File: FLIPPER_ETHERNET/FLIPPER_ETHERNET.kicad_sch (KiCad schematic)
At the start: 21 parts, among them J1 RJ45_Hanrun_HR911105A_Horizon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, J2 Conn_01x08_Socket, J3 Conn_01x10_Socket, SW1 SW_Push, U1 ENC28J60x-ML, Y1 25MHz

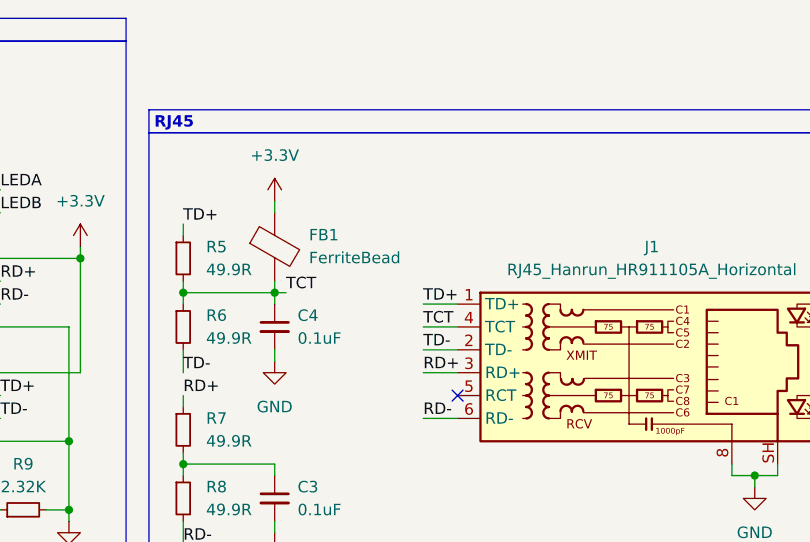
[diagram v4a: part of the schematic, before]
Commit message: feat: bom corrected and change of model components components changed were SW1 and FB1
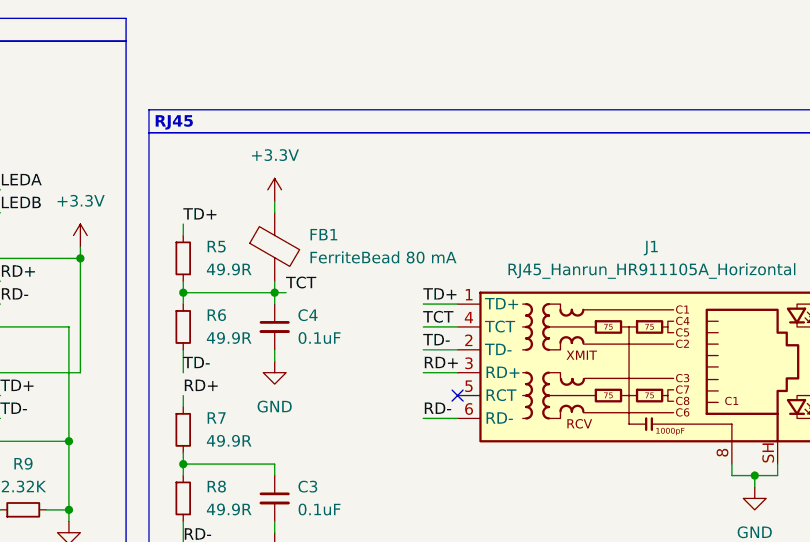
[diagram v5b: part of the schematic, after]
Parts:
- C1, C5: #LSCS C3870208 -> C107040; manf# 600S180FT250XT -> CC0603JRNPO9BN180
- C2: #LSCS C192094 -> C1691; manf# GRM188R60J106ME84D -> CL10A106MQ8NNNC
- C3, C4: #LSCS C20214933 -> C14663; manf# KGF15AR71E104JT -> CC0603KRX7R9BB104
- FB1: value FerriteBead -> FerriteBead 80 mA; footprint Inductor_SMD:L_Walsin_WLFM201209x -> FLIPPER_ETHERNET:BLM18SP221SN1B; #LSCS C6639322 -> C85824; manf# ILBB0805ER202V -> BLM18AG102SN1D
- J1: #LSCS C12074 -> C85824
- J2: #LSCS C7501580 -> C7501586; manf# PH2.54-01-02PZD -> PH2.54-01-08PZD
- J3: #LSCS C7501580 -> C7501587; manf# PH2.54-01-02PZD -> PH2.54-01-10PZD
- R1: #LSCS C6888379 -> C22775; manf# CRT0603-BY-1000ELF -> 0603WAF1000T5E
- R12, R13: #LSCS C4051836 -> C23197; manf# SFR03EZPJ510 -> 0603WAF510JT5E
- R2: #LSCS C4199414 -> C2930027; manf# CAR0603-10KB2 -> FRC0603J103TS
- R5, R6, R7, R8: #LSCS C6976359 -> C23185; manf# RMC1/16K49R9FTP -> 0603WAF499JT5E
- R9: #LSCS C4139945 -> C2933173; manf# ERJ-PA3F2321V -> FRC0603F2321TS
- SW1: footprint Button_Switch_SMD:SW_SPST_TL3342 -> Button_Switch_SMD:SW_Push_1P1T_XKB_TS-1187A; #LSCS C2886897 -> C318889; manf# TL3342F450QG -> TS-1187A-C-C-B
- U1, Y1: Proveedor LCSC -> Mouser
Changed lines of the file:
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@@
 			)
 		)
-		(property "Datasheet" "~"
+		(property "Datasheet" ""
 			(at 170.18 109.22 0)
 			(effects
@@
 			)
 		)
-		(property "#LSCS" "C6976359"
+		(property "#LSCS" "C23185"
 			(at 170.18 109.22 0)
 			(effects
@@
 			)
 		)
-		(property "manf#" "RMC1/16K49R9FTP"
+		(property "manf#" "0603WAF499JT5E"
 			(at 170.18 109.22 0)
 			(effects
@@
 			)
 		)
-		(property "Proveedor" "LCSC"
+		(property "Proveedor" "Mouser"
 			(at 52.07 123.19 0)
 			(effects
@@
 			)
 		)
-		(property "#LSCS" "C4199414"
+		(property "#LSCS" "C2930027"
 			(at 48.26 78.74 0)
 			(effects
@@
 			)
 		)
-		(property "manf#" "CAR0603-10KB2"
+		(property "manf#" "FRC0603J103TS"
 			(at 48.26 78.74 0)
 			(effects
@@
 			)
 		)
-		(property "#LSCS" "C20214933"
+		(property "#LSCS" "C14663"
 			(at 180.34 116.84 0)
 			(effects
@@
 			)
 		)
-		(property "manf#" "KGF15AR71E104JT"
+		(property "manf#" "CC0603KRX7R9BB104"
 			(at 180.34 116.84 0)
 			(effects
@@
 			)
 		)
-		(property "Datasheet" "~"
+		(property "Datasheet" "https://www.lcsc.com/datasheet/lcsc_datasheet_1811141815_HANRUN-Zhongshan-HanRun-Elec-HR911105A_C12074.pdf"
 			(at 220.98 87.63 0)
 			(effects
@@
 			)
 		)
-		(property "#LSCS" "C12074"
+		(property "#LSCS" "C85824"
 			(at 220.98 102.87 0)
 			(effects
@@
 			)
 		)
-		(property "#LSCS" "C3870208"
+		(property "#LSCS" "C107040"
 			(at 45.72 130.81 0)
 			(effects
@@
 			)
 		)
-		(property "manf#" "600S180FT250XT"
+		(property "manf#" "CC0603JRNPO9BN180"
 			(at 45.72 130.81 0)
 			(effects
@@
 			)
 		)
-		(property "#LSCS" "C7501580"
+		(property "#LSCS" "C7501587"
 			(at 82.55 118.11 0)
 			(effects
@@
 			)
 		)
-		(property "manf#" "PH2.54-01-02PZD"
+		(property "manf#" "PH2.54-01-10PZD"
 			(at 82.55 118.11 0)
 			(effects
@@
 			)
 		)
-		(property "Datasheet" "~"
+		(property "Datasheet" ""
 			(at 170.18 90.17 0)
 			(effects
@@
 			)
 		)
-		(property "#LSCS" "C6976359"
+		(property "#LSCS" "C23185"
 			(at 170.18 90.17 0)
 			(effects
@@
 			)
 		)
-		(property "manf#" "RMC1/16K49R9FTP"
+		(property "manf#" "0603WAF499JT5E"
 			(at 170.18 90.17 0)
 			(effects
@@
 			)
 		)
-		(property "Datasheet" "~"
+		(property "Datasheet" ""
 			(at 152.4 118.11 0)
 			(effects
@@
 			)
 		)
-		(property "#LSCS" "C4139945"
+		(property "#LSCS" "C2933173"
 			(at 152.4 118.11 0)
 			(effects
@@
 			)
 		)
-		(property "manf#" "ERJ-PA3F2321V"
+		(property "manf#" " FRC0603F2321TS"
 			(at 152.4 118.11 0)
 			(effects
@@
 			)
 		)
-		(property "Datasheet" "~"
+		(property "Datasheet" ""
 			(at 170.18 97.79 0)
 			(effects
@@
 			)
 		)
-		(property "#LSCS" "C6976359"
+		(property "#LSCS" "C23185"
 			(at 170.18 97.79 0)
 			(effects
@@
 			)
 		)
-		(property "manf#" "RMC1/16K49R9FTP"
+		(property "manf#" "0603WAF499JT5E"
 			(at 170.18 97.79 0)
 			(effects
@@
 			)
 		)
-		(property "Datasheet" "~"
+		(property "Datasheet" "https://ww1.microchip.com/downloads/aemDocuments/documents/OTH/ProductDocuments/DataSheets/39662e.pdf"
 			(at 130.81 102.87 0)
 			(effects
@@
 			)
 		)
-		(property "Proveedor" "LCSC"
+		(property "Proveedor" "Mouser"
 			(at 130.81 102.87 0)
 			(effects
@@
 			)
 		)
-		(property "Footprint" "Button_Switch_SMD:SW_SPST_TL3342"
+		(property "Footprint" "Button_Switch_SMD:SW_Push_1P1T_XKB_TS-1187A"
 			(at 58.42 73.66 0)
 			(effects
@@
 			)
 		)
-		(property "#LSCS" " C2886897"
+		(property "#LSCS" " C318889"
 			(at 58.42 78.74 0)
 			(effects
@@
 			)
 		)
-		(property "manf#" "TL3342F450QG"
+		(property "manf#" "TS-1187A-C-C-B"
 			(at 58.42 78.74 0)
 			(effects
@@
 			)
 		)
-		(property "Value" "FerriteBead"
+		(property "Value" "FerriteBead 80 mA"
 			(at 184.15 90.1191 0)
 			(effects
@@
 			)
 		)
-		(property "Footprint" "Inductor_SMD:L_Walsin_WLFM201209x"
+		(property "Footprint" "FLIPPER_ETHERNET:BLM18SP221SN1B"
 			(at 178.562 88.9 90)
 			(effects
@@
 			)
 		)
-		(property "#LSCS" "C6639322"
+		(property "#LSCS" "C85824"
 			(at 180.34 88.9 0)
 			(effects
@@
 			)
 		)
-		(property "manf#" "ILBB0805ER202V"
+		(property "manf#" "BLM18AG102SN1D"
 			(at 180.34 88.9 0)
 			(effects
@@
 			)
 		)
-		(property "#LSCS" "C20214933"
+		(property "#LSCS" "C14663"
 			(at 180.34 97.79 0)
 			(effects
@@
 			)
 		)
-		(property "manf#" "KGF15AR71E104JT"
+		(property "manf#" "CC0603KRX7R9BB104"
 			(at 180.34 97.79 0)
 			(effects
@@
 			)
 		)
-		(property "#LSCS" "C4051836"
+		(property "#LSCS" "C23197"
 			(at 248.92 107.95 0)
 			(effects
@@
 			)
 		)
-		(property "manf#" "SFR03EZPJ510"
+		(property "manf#" "0603WAF510JT5E"
 			(at 248.92 107.95 0)
 			(effects
@@
 			)
 		)
-		(property "#LSCS" "C4051836"
+		(property "#LSCS" "C23197"
 			(at 248.92 97.79 0)
 			(effects
@@
 			)
 		)
-		(property "manf#" "SFR03EZPJ510"
+		(property "manf#" "0603WAF510JT5E"
 			(at 248.92 97.79 0)
 			(effects
@@
 			)
 		)
-		(property "Datasheet" "~"
+		(property "Datasheet" ""
 			(at 170.18 116.84 0)
 			(effects
@@
 			)
 		)
-		(property "#LSCS" "C6976359"
+		(property "#LSCS" "C23185"
 			(at 170.18 116.84 0)
 			(effects
@@
 			)
 		)
-		(property "manf#" "RMC1/16K49R9FTP"
+		(property "manf#" "0603WAF499JT5E"
 			(at 170.18 116.84 0)
 			(effects
@@
 			)
 		)
-		(property "#LSCS" "C6888379"
+		(property "#LSCS" "C22775"
 			(at 57.15 130.81 0)
 			(effects
@@
 			)
 		)
-		(property "manf#" "CRT0603-BY-1000ELF"
+		(property "manf#" "0603WAF1000T5E"
 			(at 57.15 130.81 0)
 			(effects
@@
 			)
 		)
-		(property "Datasheet" "~"
+		(property "Datasheet" ""
 			(at 149.86 127 0)
 			(effects
@@
 			)
 		)
-		(property "#LSCS" "C192094"
+		(property "#LSCS" "C1691"
 			(at 149.86 127 0)
 			(effects
@@
 			)
 		)
-		(property "manf#" "GRM188R60J106ME84D"
+		(property "manf#" "CL10A106MQ8NNNC"
 			(at 149.86 127 0)
 			(effects
@@
 			)
 		)
-		(property "#LSCS" "C3870208"
+		(property "#LSCS" "C107040"
 			(at 45.72 118.11 0)
 			(effects
@@
 			)
 		)
-		(property "manf#" "600S180FT250XT"
+		(property "manf#" "CC0603JRNPO9BN180"
 			(at 45.72 118.11 0)
 			(effects
@@
 			)
 		)
-		(property "#LSCS" "C7501580"
+		(property "#LSCS" " C7501586"
 			(at 82.55 80.01 0)
 			(effects
@@
 			)
 		)
-		(property "manf#" "PH2.54-01-02PZD"
+		(property "manf#" " PH2.54-01-08PZD"
 			(at 82.55 80.01 0)
 			(effects

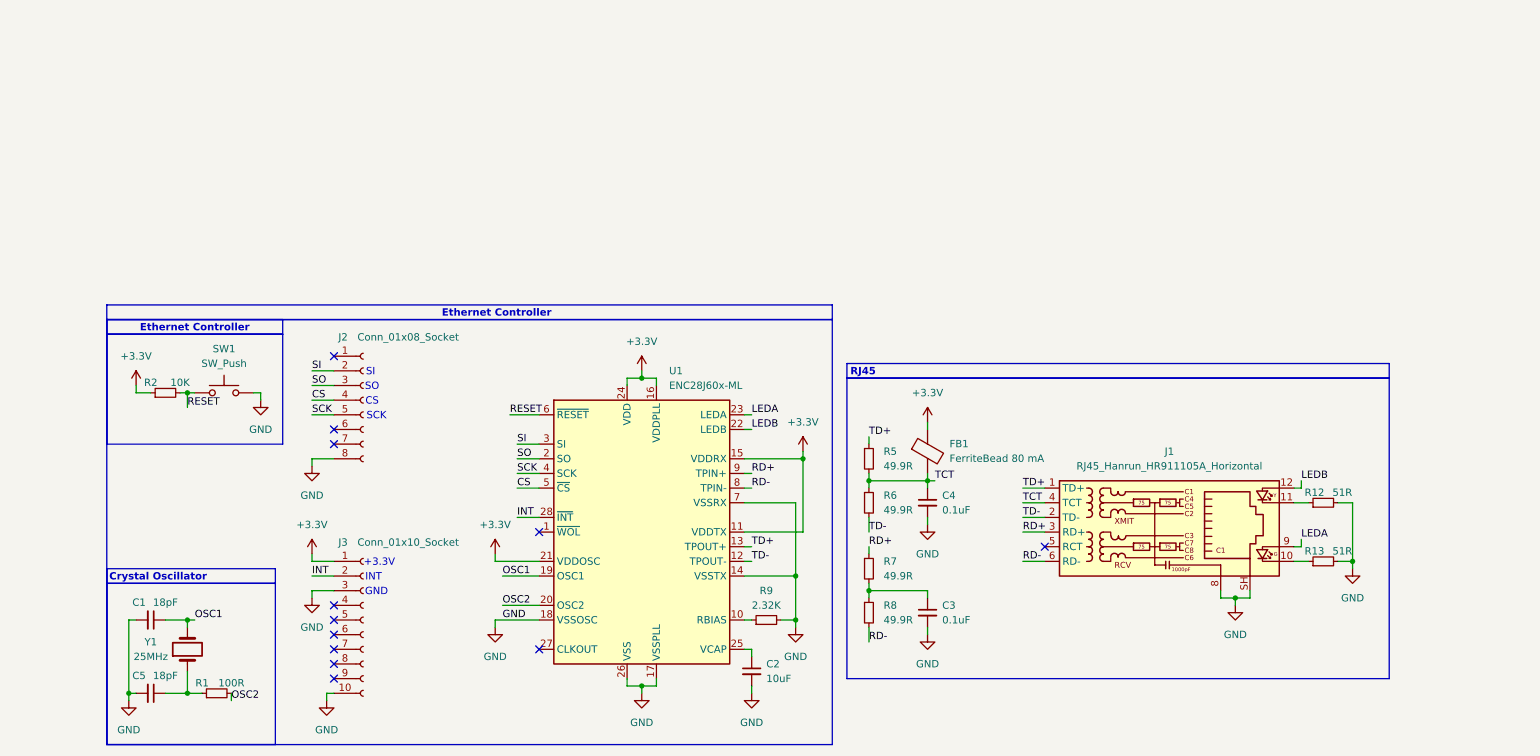
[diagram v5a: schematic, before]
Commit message: feat: flipper ethernet pcb adapted in olimex pcb
All components passed behind the pcb except the
RJ45 and reset button

Decoupling capacitors of ENC28J60 added

Crystal changed for a smaller one
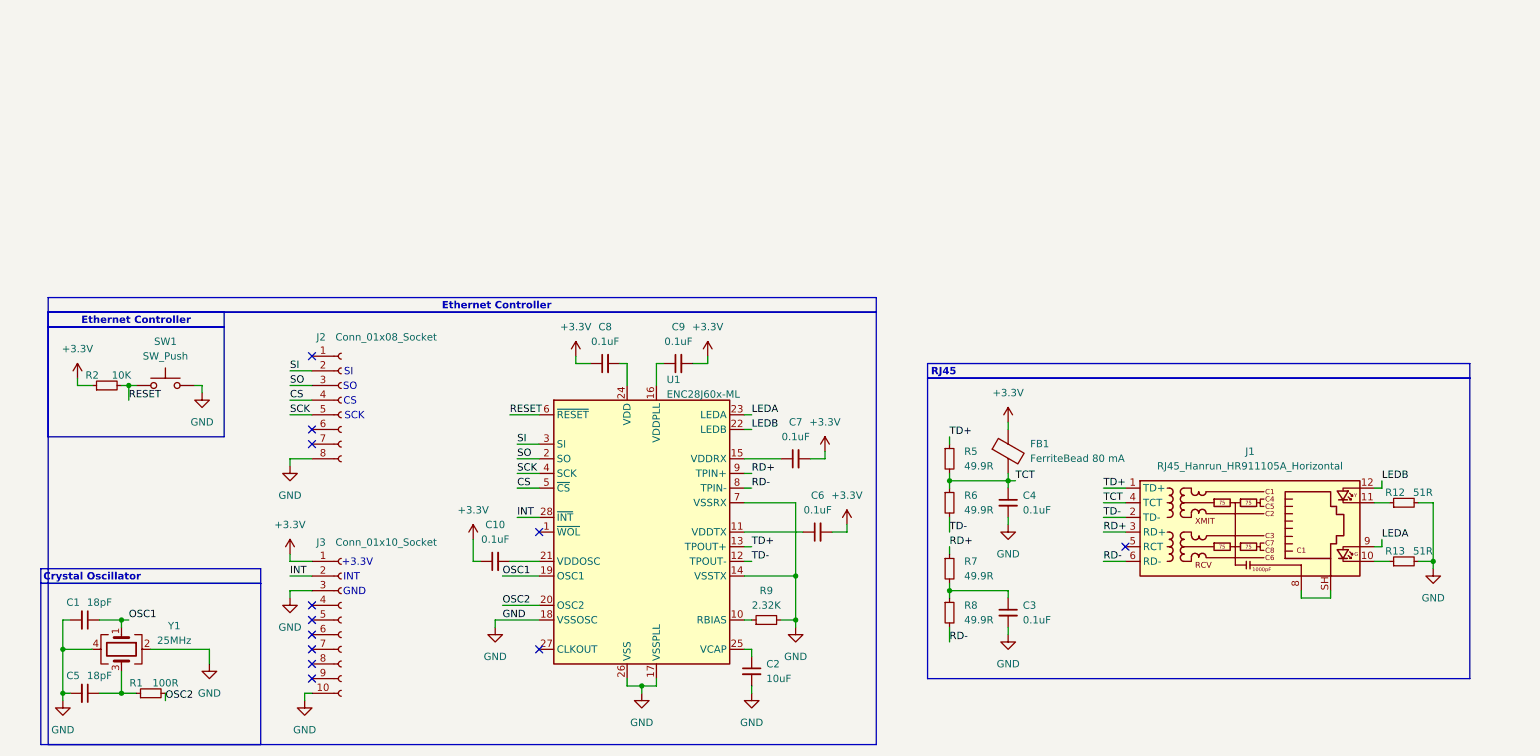
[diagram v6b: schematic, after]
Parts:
- removed Y1: 25MHz, FLIPPER_ETHERNET:ABLS-25.000MHZ-20-F-T, symbol Device:Crystal
- added C10, C6, C7, C8, C9: 0.1uF, Capacitor_SMD:C_0603_1608Metric, symbol Device:C_Small
- added Y1: 25MHz, Crystal:Crystal_SMD_SeikoEpson_FA128-4Pin_2.0x1.6mm, symbol Device:Crystal_GND24
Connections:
- net +3.3V: now also C10.1, C6.2, C7.2, C8.1, C9.2; no longer U1.11 (VDDTX), U1.15 (VDDRX), U1.16 (VDDPLL), U1.21 (VDDOSC), U1.24 (VDD)
- net GND: now also Y1.2, Y1.4; no longer J1.8, J1.SH
- net OSC1: now also Y1.1
- net at C5.1, R1.1: now also Y1.3
- new net: C8.2, U1.24 (VDD)
- new net: J1.8, J1.SH
- new net: C6.1, U1.11 (VDDTX)
- new net: C7.1, U1.15 (VDDRX)
- new net: C9.1, U1.16 (VDDPLL)
- new net: C10.2, U1.21 (VDDOSC)
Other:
- moved on the sheet: C1, C3, C4, C5, FB1, J1, J2, J3, R1, R12, R13, R2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

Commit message: feat: some pcb routes corrected
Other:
- moved on the sheet: C1, C5, R1, Y1

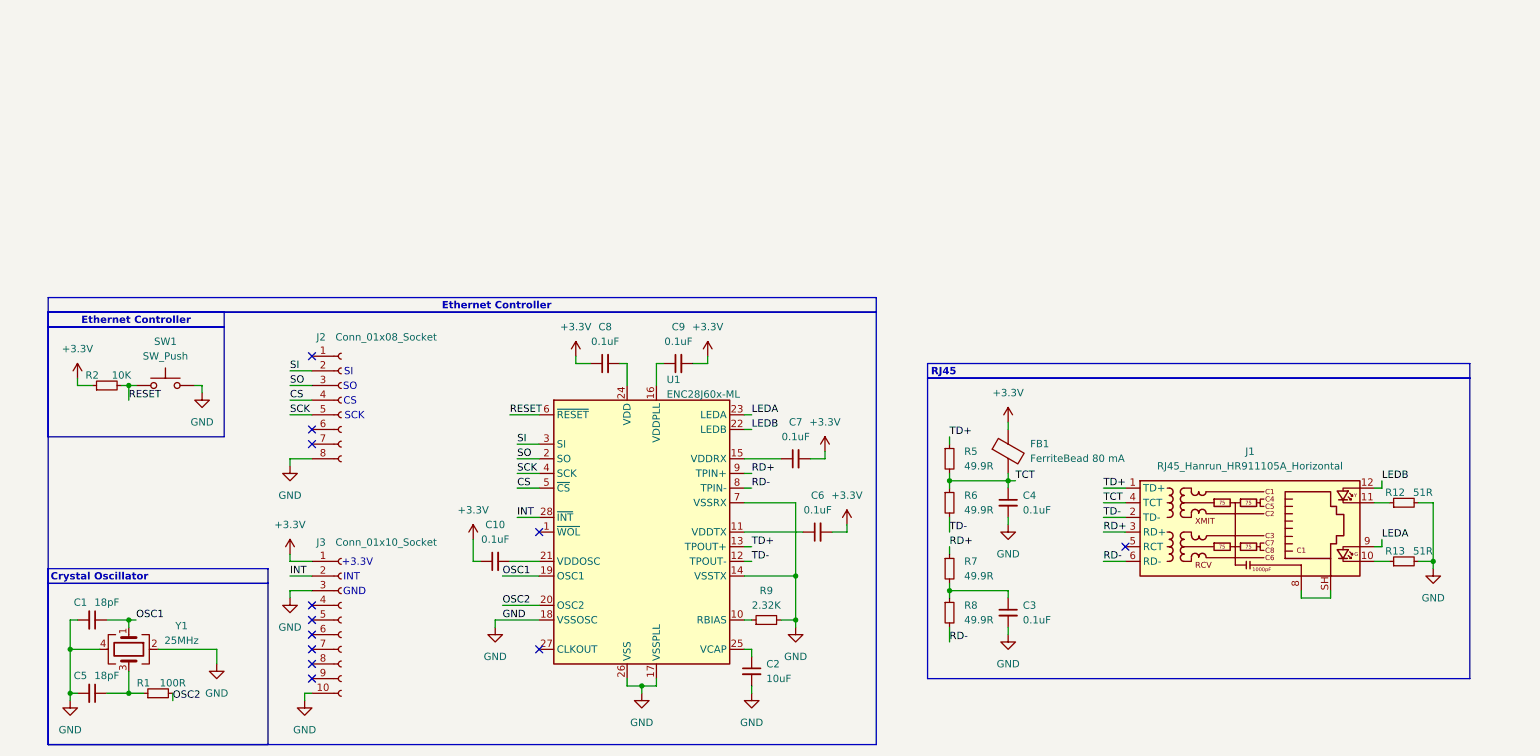
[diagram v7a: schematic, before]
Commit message: feat: flipper ethernet pcb modified
decoupling capacitor connections fixed

components moved close to the ethernet

differential pairs and other routes modified
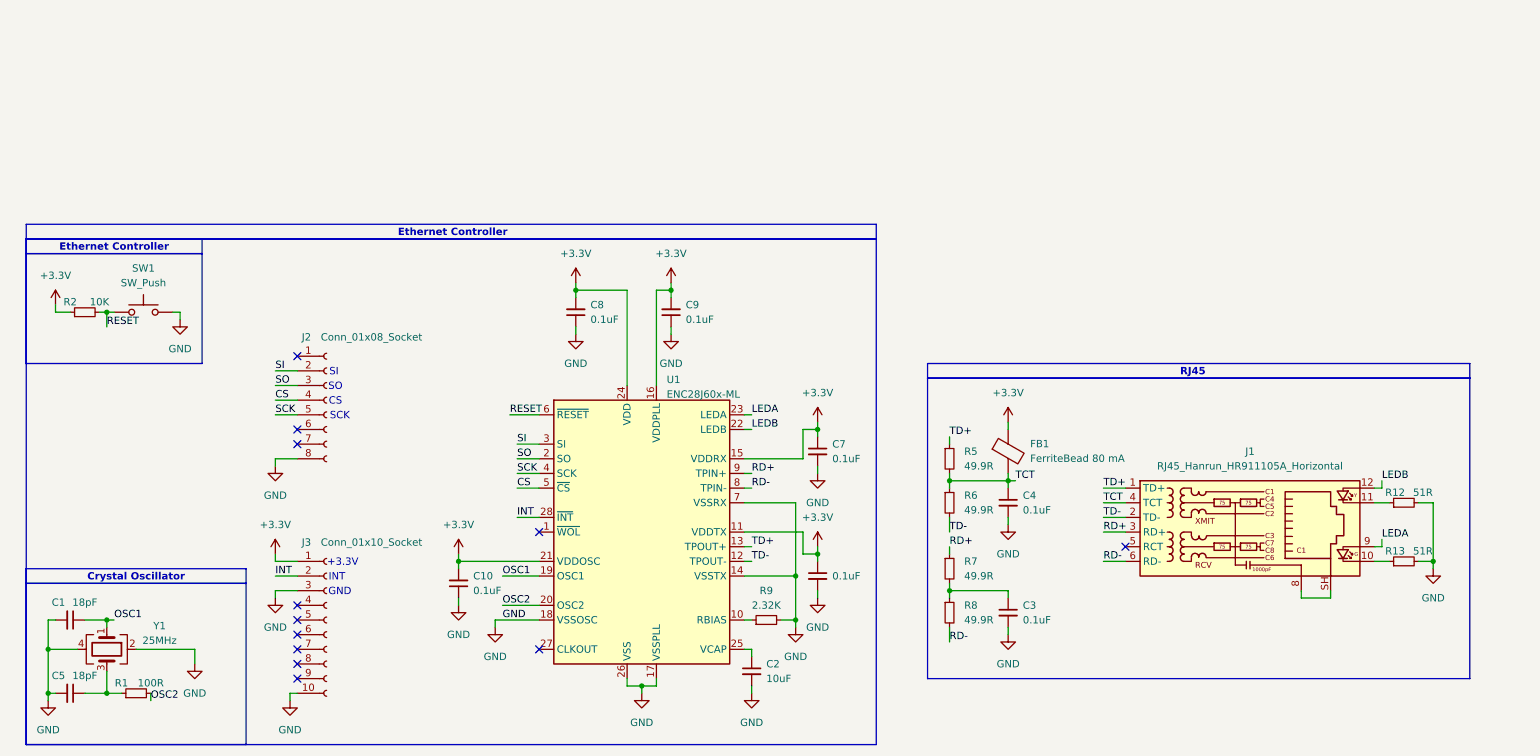
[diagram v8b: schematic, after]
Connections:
- net +3.3V: now also C10.2, C6.1, C7.1, C8.2, U1.11 (VDDTX), U1.15 (VDDRX), U1.16 (VDDPLL), U1.21 (VDDOSC), U1.24 (VDD); no longer C10.1, C6.2, C7.2, C8.1
- net GND: now also C10.1, C6.2, C7.2, C8.1, C9.1
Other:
- moved on the sheet: C1, C10, C5, C7, C8, C9, J2, J3, R1, R2, SW1, Y1
